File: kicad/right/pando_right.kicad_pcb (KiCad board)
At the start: 2 copper layers, 144.1 x 121.5 mm, 71 parts, among them J1 USB_C_Receptacle_USB2.0_14P, U1 PCA9555PW, U2 PRTR5V0U2X

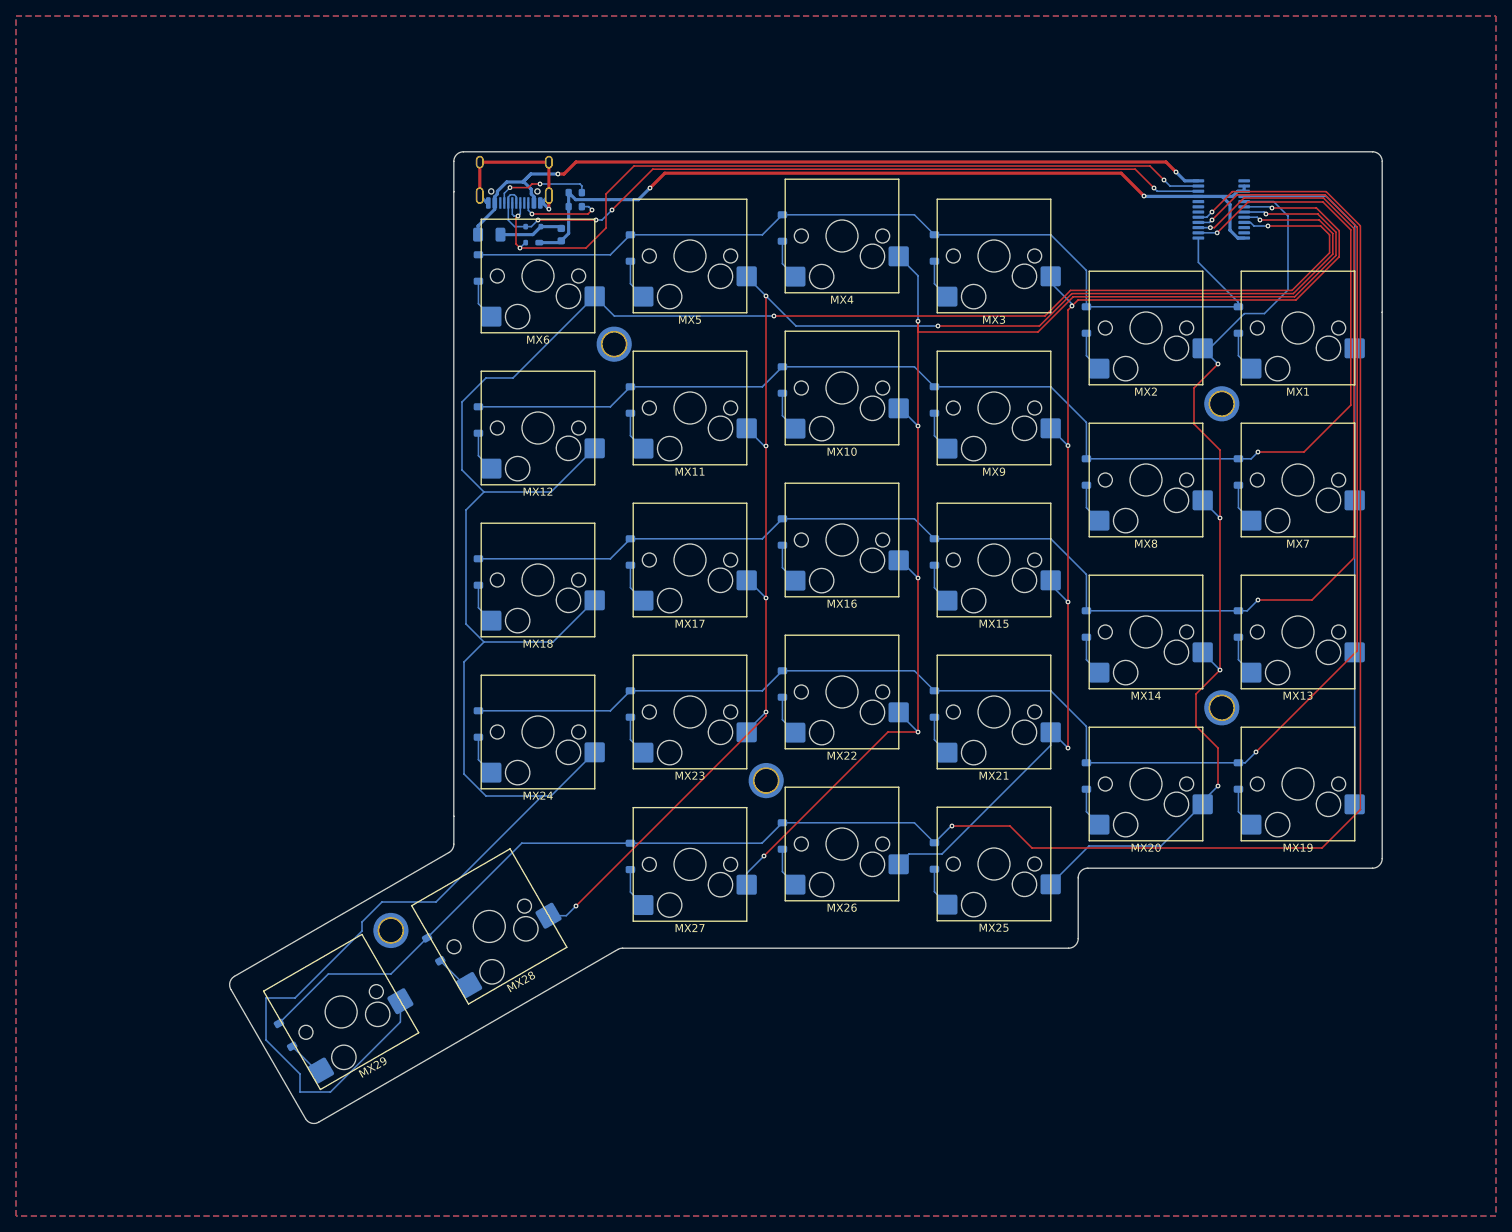
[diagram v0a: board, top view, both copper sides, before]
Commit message: v1.1.0: Fix I2C pull-up routing and clean up traces
- Reposition I2C pull-up resistors R7/R8 with VBUS connections
- Clean up DATA0/DATA1 label positions and wire routing
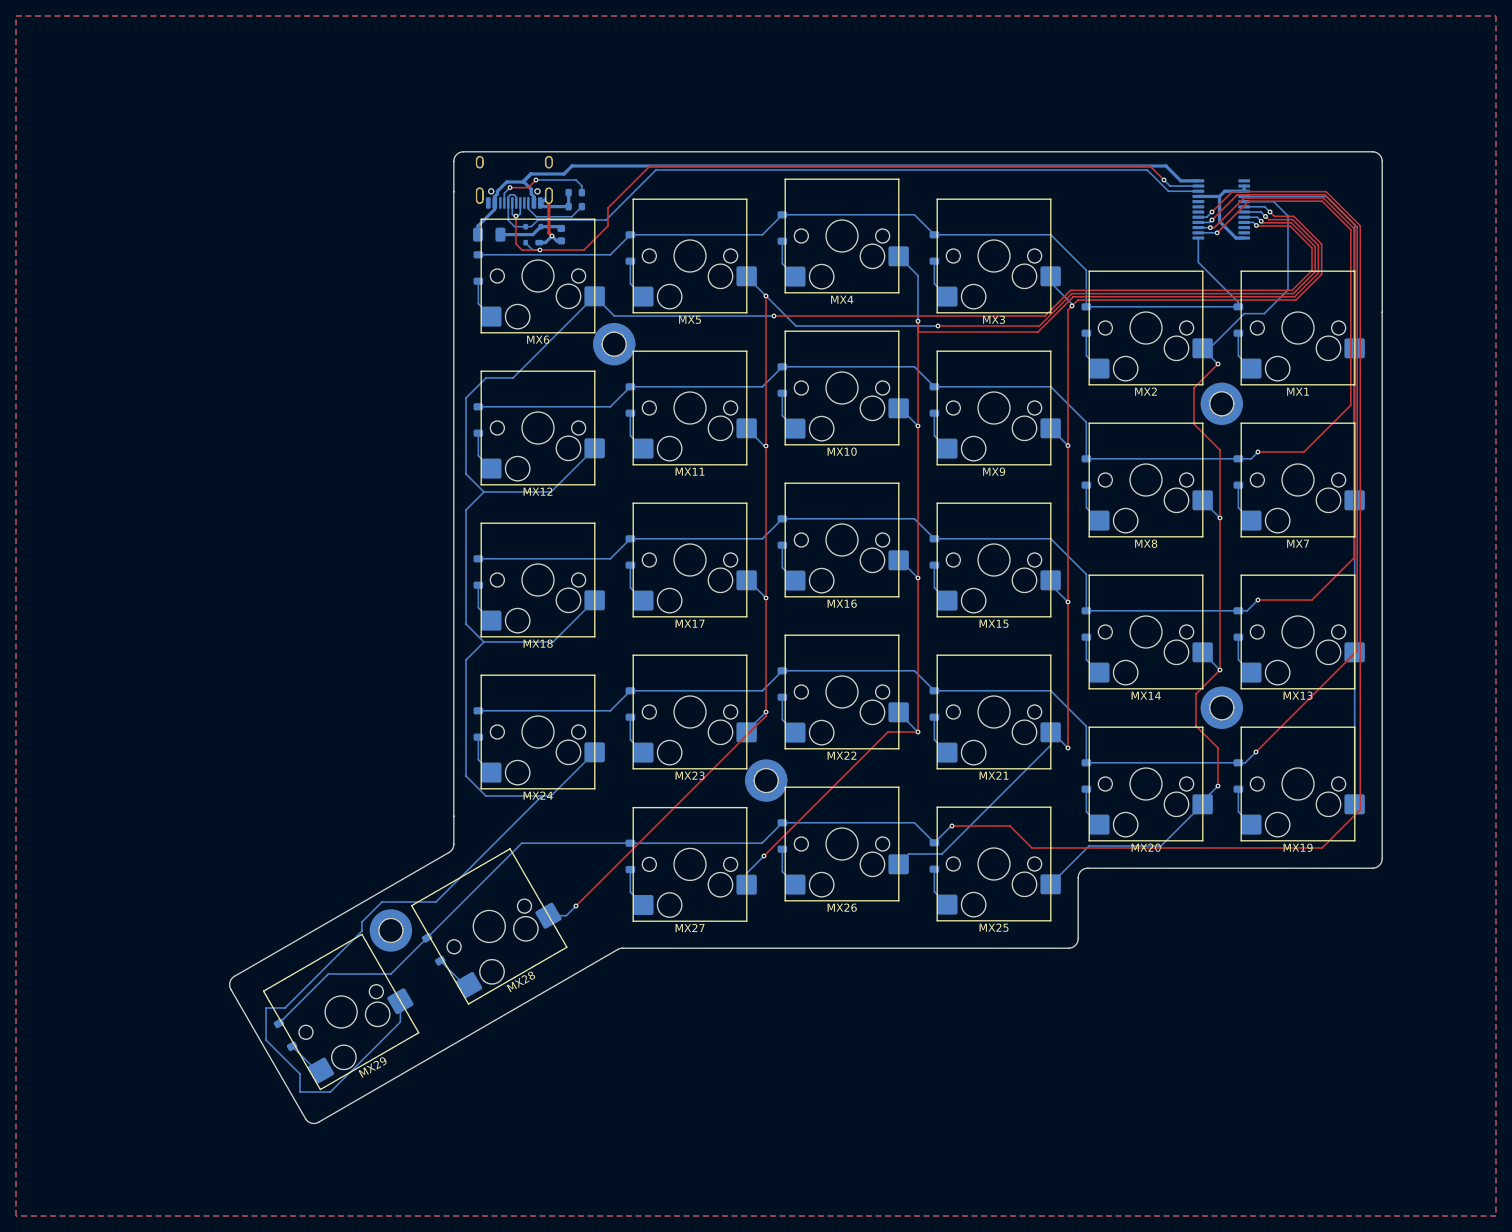
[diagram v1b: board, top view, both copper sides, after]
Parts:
- H1, H2, H3, H4, H5: footprint Pando:MountingHole_2.9mm_M2_Pad_TopOnly -> Mounting_Wuerth:Mounting_Wuerth_WA-SMSI-M2_H3.5mm_9774035243
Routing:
- net GND: track 127.0 -> 29.2 mm, vias 3 -> 1
- net COL5: track 312.0 -> 306.6 mm
- net COL3: track 173.2 -> 169.1 mm
- net COL2: track 147.5 -> 143.4 mm
- net COL4: track 193.9 -> 189.9 mm
- net Net-(J1-CC2): track 10.7 -> 8.36 mm, vias 2 -> 0
- net VBUS: track 101.0 -> 100.6 mm, vias 2 -> 0
- net DATA0: track 95.6 -> 95.5 mm, vias 4 -> 0
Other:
- board text added: "Designed in Washington, USA - by jyap - v1.1"
- board text removed: "Designed in Washington, USA - by jyap - v1.0"
